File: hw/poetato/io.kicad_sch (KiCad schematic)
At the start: 41 parts, among them J1 1757349, J2 1757268, Q6 NTK3134N, T1 1308_750319693, U15 SN6507DGQR, U19 TPS26625DRCR

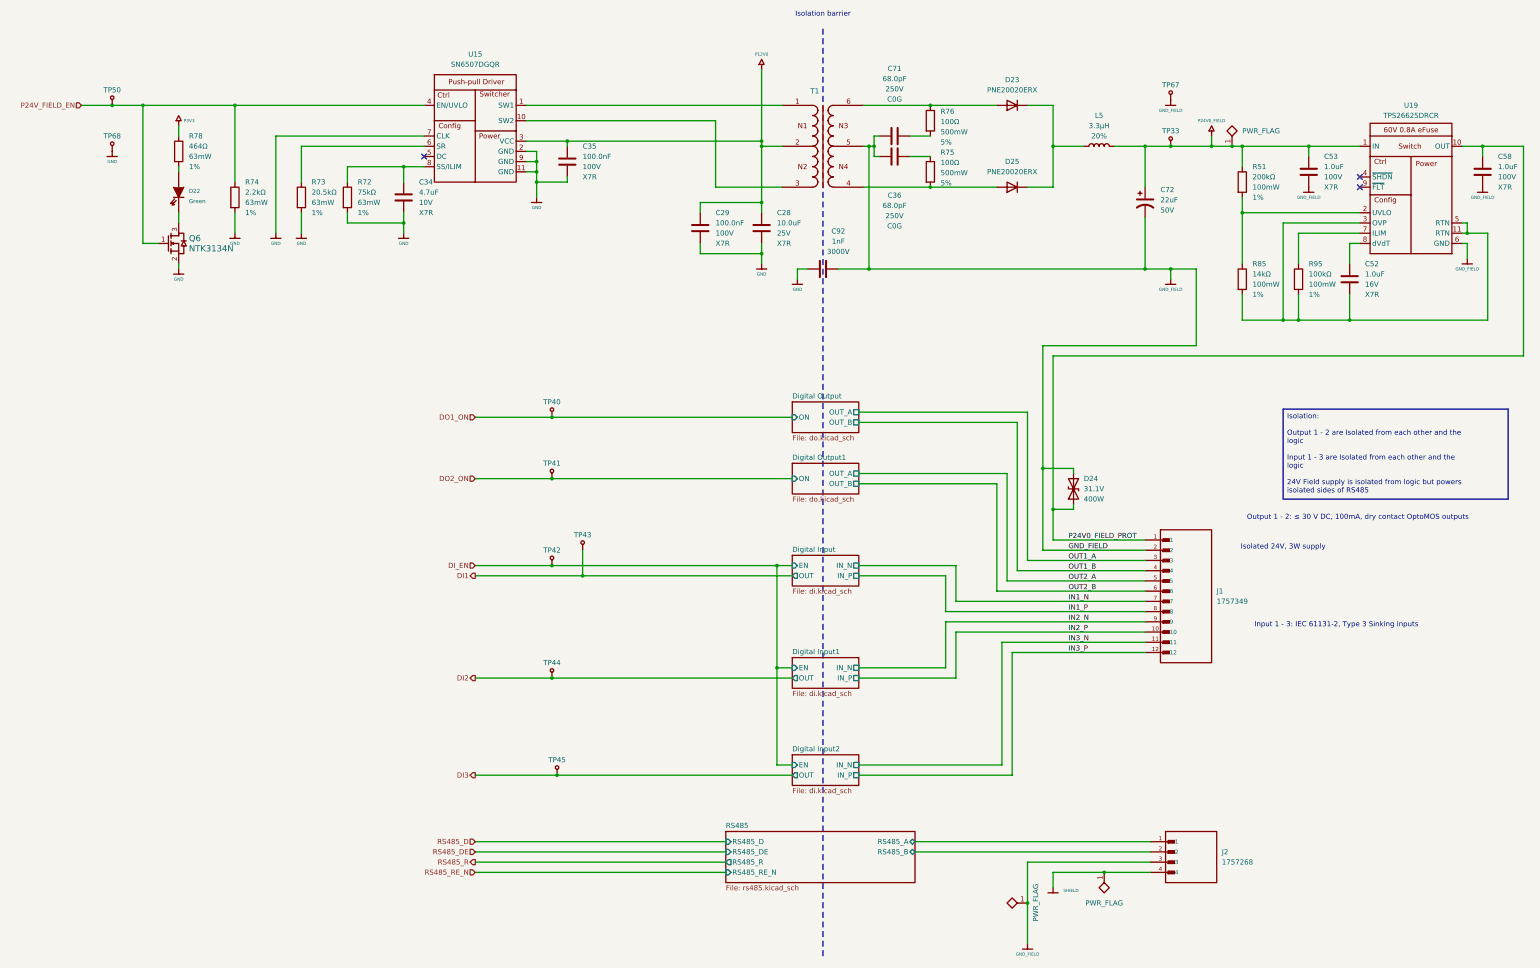
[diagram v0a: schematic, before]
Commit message: hw: sync symbols with kicadlib field text and value updates
Update Symbols from Library for kicadlib 8686346 (field text 1.27 mm) and
5b35b6c (units on misc R/C values). Value text sizes synced to the library
by script, since a Value reset would also reset power-symbol net names.
Restored BOM_Entry Manufacturer/Part Number and the R57 Power field that the
update cleared, and field positions it reset. Nudged R1, C6, Q6 and C75 text
clear of the larger power-symbol labels. ERC clean, netlist unchanged apart
from the intended values.
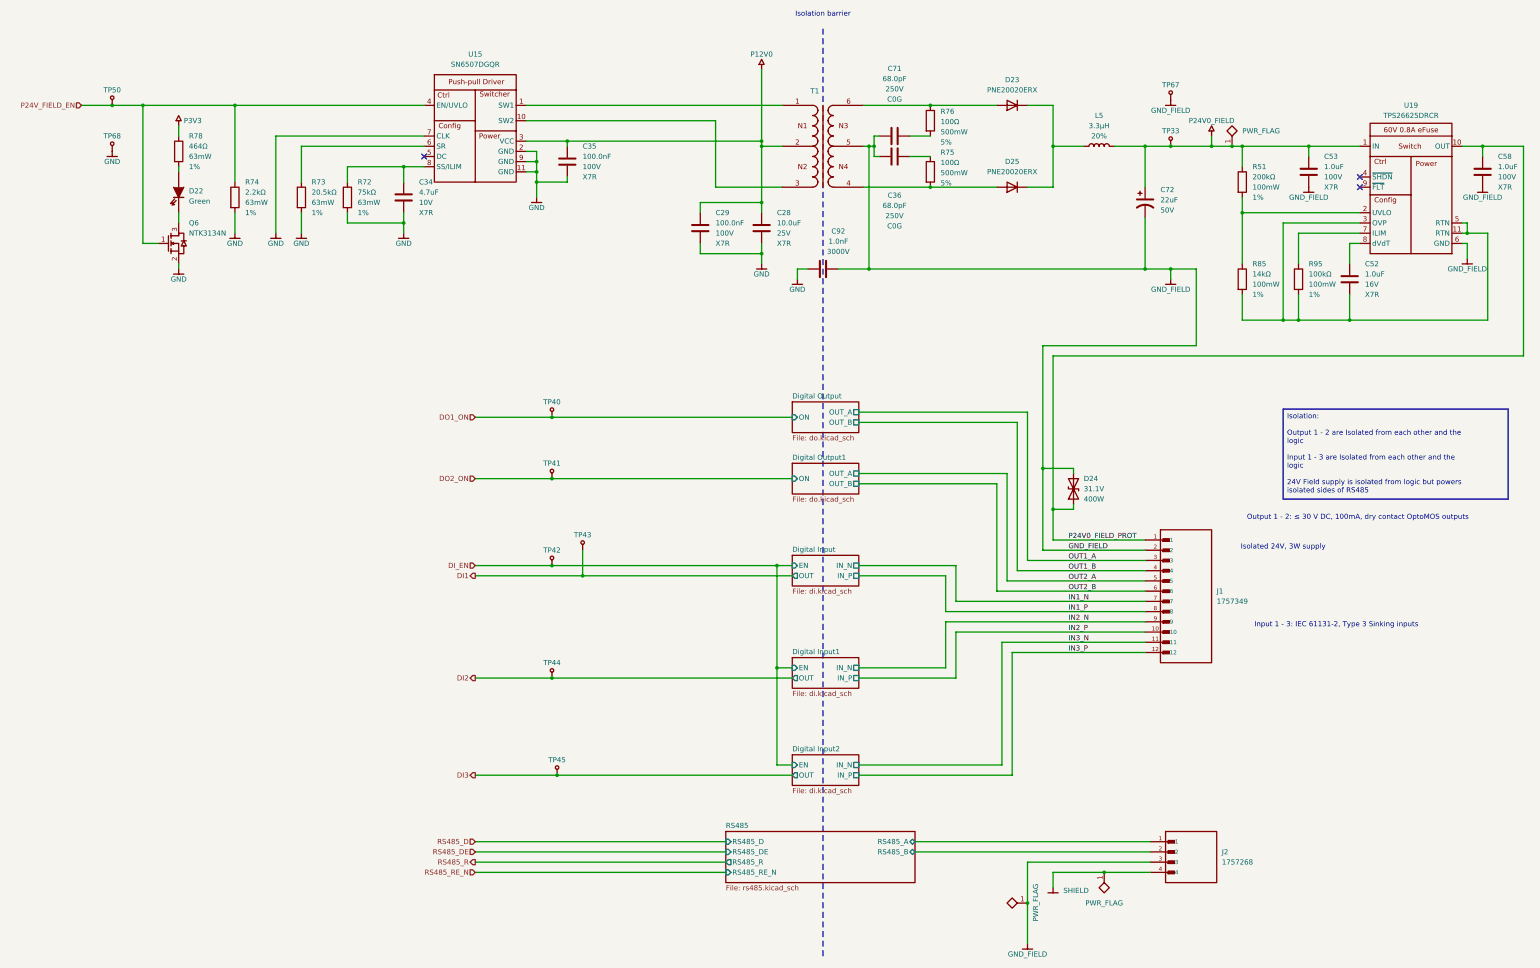
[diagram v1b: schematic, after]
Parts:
- C92: value 1nF -> 1.0nF

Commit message: hw: rename IO sub-sheets DO1/DO2/DI1-DI3 and order their pages
The old names were off by one against the channel numbers ("Digital
Output1" was DO2). Pages now run DO1, DO2, DI1, DI2, DI3 instead of
interleaving. Sheet UUIDs are unchanged; only the three COOL_POUR nets
change name.
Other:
- sheet Digital Input renamed DI1
- sheet Digital Input1 renamed DI2
- sheet Digital Input2 renamed DI3
- sheet Digital Output renamed DO1
- sheet Digital Output1 renamed DO2
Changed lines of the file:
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@@
 			(color 0 0 0 0)
 		)
-		(property "Sheetname" "Digital Input2"
+		(property "Sheetname" "DI3"
 			(at 212.09 198.6784 0)
 			(show_name no)
@@
 			(color 0 0 0 0)
 		)
-		(property "Sheetname" "Digital Output1"
+		(property "Sheetname" "DO2"
 			(at 212.09 126.2884 0)
 			(show_name no)
@@
 			(project "poetato"
 				(path "/f0f504bb-124c-46e5-ad39-032d3dfa78b3/7f50897c-81bd-4425-95ed-f5153c9db421"
-					(page "8")
+					(page "7")
 				)
 			)
@@
 			(color 0 0 0 0)
 		)
-		(property "Sheetname" "Digital Input"
+		(property "Sheetname" "DI1"
 			(at 212.09 149.1484 0)
 			(show_name no)
@@
 			(project "poetato"
 				(path "/f0f504bb-124c-46e5-ad39-032d3dfa78b3/7f50897c-81bd-4425-95ed-f5153c9db421"
-					(page "7")
+					(page "8")
 				)
 			)
@@
 			(color 0 0 0 0)
 		)
-		(property "Sheetname" "Digital Output"
+		(property "Sheetname" "DO1"
 			(at 212.09 111.0484 0)
 			(show_name no)
@@
 			(color 0 0 0 0)
 		)
-		(property "Sheetname" "Digital Input1"
+		(property "Sheetname" "DI2"
 			(at 212.09 174.5484 0)
 			(show_name no)

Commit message: hw: move the DC/DC converters to a new top-level Power sheet
power.kicad_sch (page 4) holds the 3.3 V buck (from MCU), the isolated
24 V field supply with its enable FET and LED (from IO) and the RS-485
5 V buck (from RS485). The two bucks are mirrored to read left to right.
The PoE flyback stays on the Ethernet sheet.

P5V_RS485 is now a power symbol and P24V_FIELD_EN goes from MCU to the
Power sheet at the top level. On IO the eFuse moved next to J1, removing
the output loop around the page. The power tree is redrawn more compact
to make room for the new sheet symbol.

Symbols keep their UUIDs and references. ERC clean; every net connects
the same pins as before, 7 nets renamed by the new sheet path.
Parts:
- removed C28: ${Capacitance}, Capacitor_SMD:C_0805_2012Metric, symbol cap_mlcc_murata_GRM:GRM/C0805_10u_25V_X7R_10%
- removed C29, C35: ${Capacitance}, Capacitor_SMD:C_0603_1608Metric, symbol cap_mlcc_murata_GRM:GRM/C0603_100n_100V_X7R_10%
- removed C34: ${Capacitance}, Capacitor_SMD:C_0603_1608Metric, symbol cap_mlcc_murata_GRM:GRM/C0603_4u7_10V_X7R_10%
- removed C36, C71: ${Capacitance}, Capacitor_SMD:C_0603_1608Metric, symbol cap_rfmw_murata_gqm:GQM/C0603_68p_250V_C0G_5%
- removed C72: ${Capacitance}, Capacitor_SMD:CP_Elec_5x5.8, symbol cap_alel_chemicon:AlEl/C5x5.8_22u_50V_MZR_20
- removed C92: 1.0nF, Capacitor_SMD:C_1808_4520Metric, symbol misc_capacitors:C1808_1n_3000V_X7R_10
- removed D22: LED0402_150040VS73240, LED_SMD:LED_0402_1005Metric, symbol LEDs:LED0402_150040VS73240
- removed D23, D25: PNE20020ERX, Diode_SMD:Nexperia_CFP3_SOD-123W, symbol diode_misc:PNE20020ERX
- removed L5: 3.3µH, Jonas:IHLP1212BZ, symbol ind_power_vishay_ihlp:IHLP/L1212_3u3_20_4A5
- removed Q6: NTK3134N, Package_TO_SOT_SMD:SOT-723, symbol transistors:NTK3134N
- removed R72: 75kΩ, Resistor_SMD:R_0402_1005Metric, symbol res_chip_vishay_crcw:CRCW/R0402_75k0_1_63mW
- removed R73: 20.5kΩ, Resistor_SMD:R_0402_1005Metric, symbol res_chip_vishay_crcw:CRCW/R0402_20k5_1_63mW
- removed R74: 2.2kΩ, Resistor_SMD:R_0402_1005Metric, symbol res_chip_vishay_crcw:CRCW/R0402_2k2_1_63mW
- removed R75, R76: 100Ω, Resistor_SMD:R_1210_3225Metric, symbol res_pulse_panasonic_erj14t:ERJ-T14/R1210_100R0_5_500mW
- removed R78: 464Ω, Resistor_SMD:R_0402_1005Metric, symbol res_chip_vishay_crcw:CRCW/R0402_464R0_1_63mW
- removed T1: 1308_750319693, Jonas:T_Wurth_WE-PPTI-1308, symbol misc_inductors:1308_750319693
- removed TP33, TP50, TP67, TP68: TP, TestPoint:TestPoint_Pad_D1.0mm, symbol power:TP
- removed U15: SN6507DGQR, Package_SO:HVSSOP-10-1EP_3x3mm_P0.5mm_EP1.83x1.89mm, symbol dcdc:SN6507DGQR
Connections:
- no-connect marks 3 -> 2
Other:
- note removed: "Isolated 24V, 3W supply"
- title: PoEtato - Field I/O, isolated 24 V supply -> PoEtato - Field I/O
- moved on the sheet: C52, C53, C58, R51, R85, R95, U19
